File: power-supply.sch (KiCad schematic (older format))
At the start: 90 parts, among them IC1 TPS54561, J11 DC_SOCKET, J12 S2B-PH-K-S_LF__SN_, U10 TPS62823DLCT, U11 TPS62823DLCT, U12 TPS62823DLCT, U13 TPS62823DLCT, U9 LM3881MME_NOPB

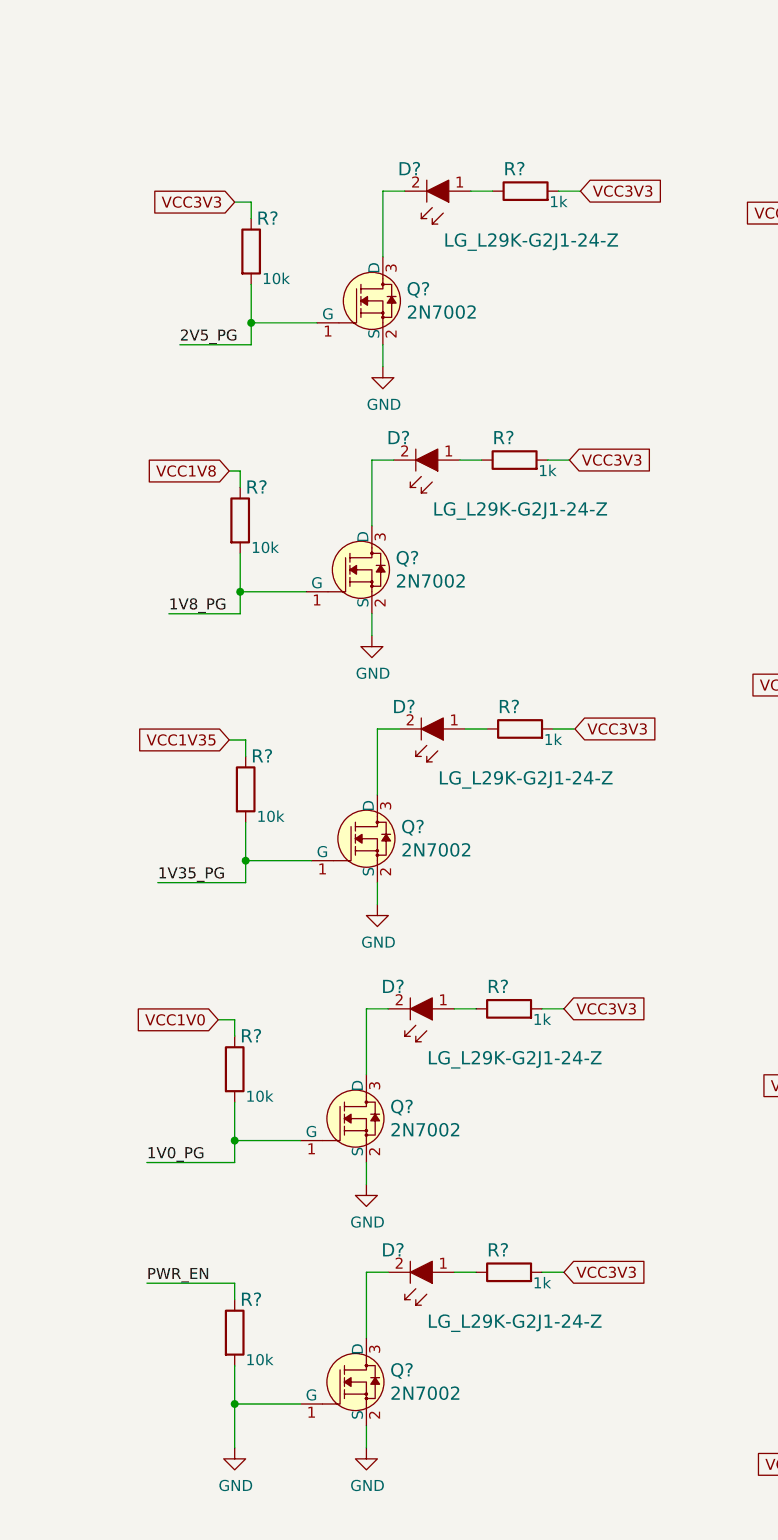
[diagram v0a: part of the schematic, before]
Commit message: Added VRs component placement, fix in 5V0 layout
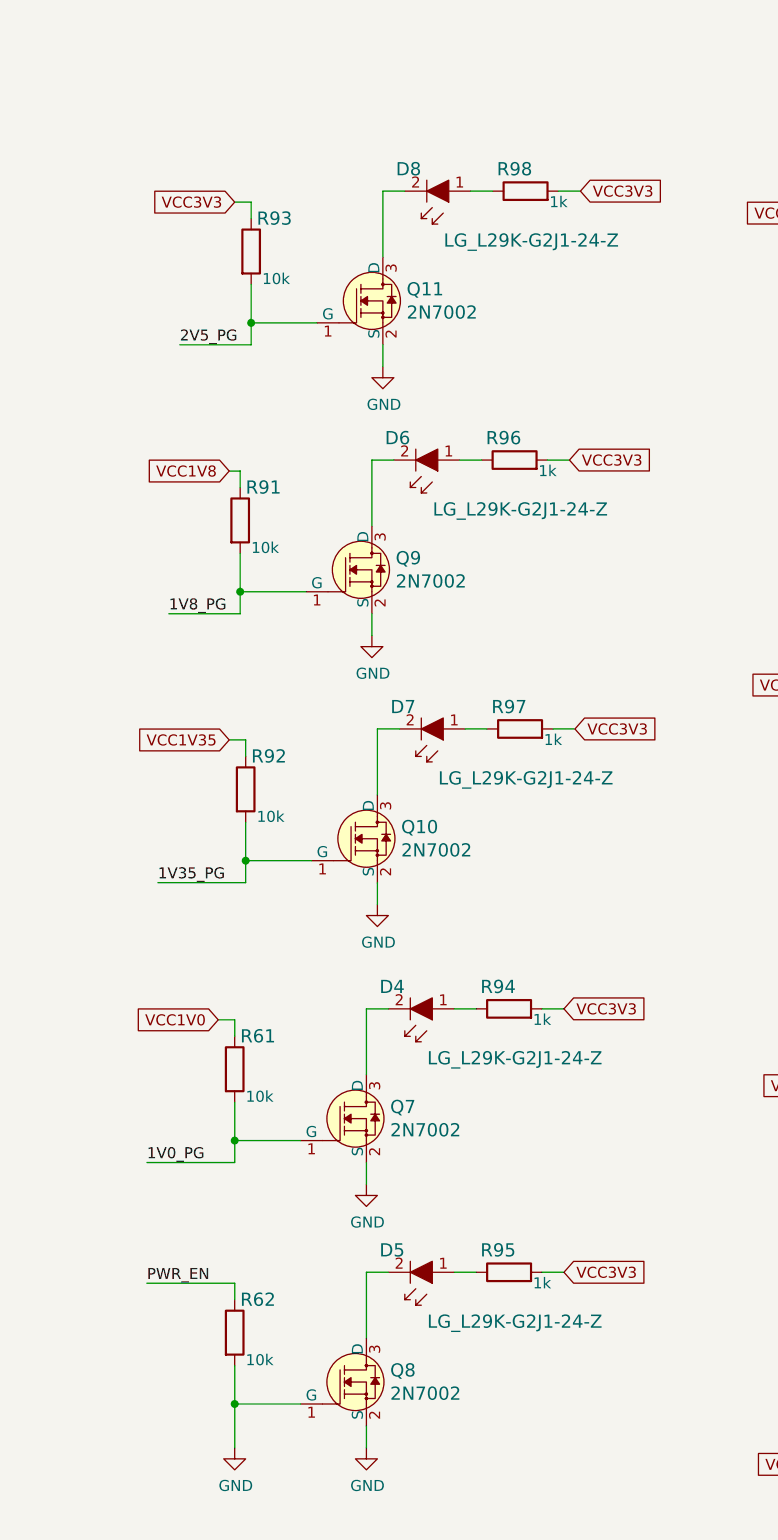
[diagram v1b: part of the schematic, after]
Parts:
- removed R69: R_0R_0402, artix-dc-scm-footprints:0402-res, symbol artix-dc-scm:R_0R_0402
- added R69: R_0R_1206, artix-dc-scm-footprints:1206-res, symbol artix-dc-scm:R_0R_1206
- gave numbers to parts that had none: 28

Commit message: Removed DC connector
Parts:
- removed F2: 0466003.NR, artix-dc-scm-footprints:1206-Fuse-Littelfuse-0466-0-0-MFG, symbol artix-dc-scm:0466003.NR
- removed J11: DC_SOCKET, artix-dc-scm-footprints:DC_SOCKET, symbol artix-dc-scm:DC_SOCKET
- added TP3, TP4: RCW-0C, artix-dc-scm-footprints:PROBE_PAD_1206, symbol artix-dc-scm:RCW-0C
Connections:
- net labels added: P12V_AUX
- net labels removed: PCIe_12V
- wire segments 342 -> 337
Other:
- note added: "External 12V supply"
- note removed: "12V/2.5A\ninput"
- note removed: "fit socket but\nno fuse, optional\nfor PCIe power"
- note removed: "in socket"
- moved on the sheet: F1
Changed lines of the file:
@@
 Comment4 ""
 $EndDescr
-Text GLabel 1350 1975 0    50   Input ~ 0
-PCIe_12V
-Text Notes 1775 1250 0    50   ~ 0
-in socket
-Text Notes 1550 2275 0    50   ~ 0
-fit socket but\nno fuse, optional\nfor PCIe power
-Text Notes 1025 1550 0    50   ~ 0
-12V/2.5A\ninput
 Wire Wire Line
 	12975 2900 12675 2900
@@
 L artix-dc-scm:0466003.NR F1
 U 1 1 5FE8C269
-P 1500 1975
-F 0 "F1" H 1850 2189 50  0000 C CNN
-F 1 "0466003.NR" H 1850 2098 50  0000 C CNN
-F 2 "artix-dc-scm-footprints:1206-Fuse-Littelfuse-0466-0-0-MFG" H 1500 2275 50  0001 L CNN
-F 3 "https://www.littelfuse.com/~/media/electronics/datasheets/fuses/littelfuse_fuse_466_datasheet.pdf.pdf" H 1500 2475 50  0001 L CNN
-F 4 "Littelfuse" H 1500 2475 50  0001 L CNN "Manufacturer"
-F 5 "0466003.NR " H 1750 2375 50  0001 C CNN "MPN"
-	1    1500 1975
-	1    0    0    -1
-$EndComp
-Wire Wire Line
-	2150 1150 2275 1150
-Wire Wire Line
-	1350 1975 1600 1975
-Wire Wire Line
-	2100 1975 2350 1975
-$Comp
-L artix-dc-scm:0466003.NR F2
-U 1 1 5FFF57DB
-P 1550 1150
-F 0 "F2" H 1900 1364 50  0000 C CNN
-F 1 "0466003.NR" H 1900 1273 50  0000 C CNN
-F 2 "artix-dc-scm-footprints:1206-Fuse-Littelfuse-0466-0-0-MFG" H 1550 1450 50  0001 L CNN
-F 3 "https://www.littelfuse.com/~/media/electronics/datasheets/fuses/littelfuse_fuse_466_datasheet.pdf.pdf" H 1550 1650 50  0001 L CNN
-F 4 "Littelfuse" H 1550 1650 50  0001 L CNN "Manufacturer"
-F 5 "0466003.NR " H 1800 1550 50  0001 C CNN "MPN"
-	1    1550 1150
-	1    0    0    -1
-$EndComp
-Text GLabel 2350 1975 2    50   Input ~ 0
+P 1775 2250
+F 0 "F1" H 2125 2464 50  0000 C CNN
+F 1 "0466003.NR" H 2125 2373 50  0000 C CNN
+F 2 "artix-dc-scm-footprints:1206-Fuse-Littelfuse-0466-0-0-MFG" H 1775 2550 50  0001 L CNN
+F 3 "https://www.littelfuse.com/~/media/electronics/datasheets/fuses/littelfuse_fuse_466_datasheet.pdf.pdf" H 1775 2750 50  0001 L CNN
+F 4 "Littelfuse" H 1775 2750 50  0001 L CNN "Manufacturer"
+F 5 "0466003.NR " H 2025 2650 50  0001 C CNN "MPN"
+	1    1775 2250
+	1    0    0    -1
+$EndComp
+Wire Wire Line
+	1625 2250 1875 2250
+Wire Wire Line
+	2375 2250 2625 2250
+Text GLabel 2625 2250 2    50   Input ~ 0
 VCC12V
-Text GLabel 2400 850  2    50   Input ~ 0
-VCC12V
-Wire Wire Line
-	2275 850  2275 1150
-Wire Wire Line
-	2275 850  2400 850
-$Comp
-L artix-dc-scm:GND #PWR049
-U 1 1 60217368
-P 2300 1450
-F 0 "#PWR049" H 2300 1200 50  0001 C CNN
-F 1 "GND" H 2305 1277 50  0000 C CNN
-F 2 "" H 2300 1450 50  0001 C CNN
-F 3 "" H 2300 1450 50  0001 C CNN
-	1    2300 1450
-	1    0    0    -1
-$EndComp
 $Comp
 L artix-dc-scm:TPS54561 IC1
@@
 Text Notes 12900 6375 0    118  ~ 0
 1V35 supply
-$Comp
-L artix-dc-scm:DC_SOCKET J11
-U 1 1 633BB6FF
-P 1250 1250
-F 0 "J11" H 1183 1603 60  0000 C CNN
-F 1 "DC_SOCKET" H 1300 975 60  0001 C CNN
-F 2 "artix-dc-scm-footprints:DC_SOCKET" H 1300 900 60  0001 C CNN
-F 3 "" H 1250 1250 60  0001 C CNN
-F 4 "Multicomp" H 1275 775 50  0001 C CNN "Manufacturer"
-F 5 "MJ-179PH" H 1183 1505 50  0000 C CNN "MPN"
-	1    1250 1250
-	1    0    0    -1
-$EndComp
-Wire Wire Line
-	1650 1150 1450 1150
-Wire Wire Line
-	1450 1350 1550 1350
-Wire Wire Line
-	2300 1350 2300 1450
-Wire Wire Line
-	1450 1250 1550 1250
-Wire Wire Line
-	1550 1250 1550 1350
-Connection ~ 1550 1350
-Wire Wire Line
-	1550 1350 2300 1350
 $Comp
 L artix-dc-scm:IHLP1212AEERR47M11 L2
@@
 	0    1    1    0
 $EndComp
+$Comp
+L artix-dc-scm:RCW-0C TP3
+U 1 1 5FE83A9D
+P 1900 1575
+F 0 "TP3" V 1900 1400 50  0000 C CNN
+F 1 "RCW-0C" V 1766 1622 50  0001 C CNN
+F 2 "artix-dc-scm-footprints:PROBE_PAD_1206" H 2100 1775 60  0001 L CNN
+F 3 "https://www.te.com/commerce/DocumentDelivery/DDEController?Action=srchrtrv&DocNm=1773266&DocType=DS&DocLang=English" H 2100 1875 60  0001 L CNN
+F 4 "RCW-0C" H 2100 2075 60  0001 L CNN "MPN"
+F 5 "TE Connectivity AMP Connectors" H 2100 2675 60  0001 L CNN "Manufacturer"
+	1    1900 1575
+	0    1    1    0
+$EndComp
+$Comp
+L artix-dc-scm:RCW-0C TP4
+U 1 1 5FEA4BA8
+P 1900 1725
+F 0 "TP4" V 1925 1550 50  0000 C CNN
+F 1 "RCW-0C" V 1766 1772 50  0001 C CNN
+F 2 "artix-dc-scm-footprints:PROBE_PAD_1206" H 2100 1925 60  0001 L CNN
+F 3 "https://www.te.com/commerce/DocumentDelivery/DDEController?Action=srchrtrv&DocNm=1773266&DocType=DS&DocLang=English" H 2100 2025 60  0001 L CNN
+F 4 "RCW-0C" H 2100 2225 60  0001 L CNN "MPN"
+F 5 "TE Connectivity AMP Connectors" H 2100 2825 60  0001 L CNN "Manufacturer"
+	1    1900 1725
+	0    1    1    0
+$EndComp
+Text GLabel 2250 1400 1    50   Input ~ 0
+VCC12V
+Wire Wire Line
+	2000 1575 2250 1575
+Wire Wire Line
+	2250 1575 2250 1400
+$Comp
+L artix-dc-scm:GND #PWR?
+U 1 1 5FEC5E7F
+P 2250 1825
+F 0 "#PWR?" H 2250 1575 50  0001 C CNN
+F 1 "GND" H 2255 1652 50  0000 C CNN
+F 2 "" H 2250 1825 50  0001 C CNN
+F 3 "" H 2250 1825 50  0001 C CNN
+	1    2250 1825
+	1    0    0    -1
+$EndComp
+Wire Wire Line
+	2000 1725 2250 1725
+Wire Wire Line
+	2250 1725 2250 1825
+Text GLabel 1625 2250 0    50   Input ~ 0
+P12V_AUX
+Text Notes 1300 925  0    118  ~ 0
+External 12V supply
 $EndSCHEMATC

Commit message: Added PWR_EN optional pullup
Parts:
- added R99: R_1k_0402, artix-dc-scm-footprints:0402-res, symbol artix-dc-scm:R_1k_0402
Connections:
- net labels removed: VCCAUX_EN_N, VCCINT_EN_N, VCCIO_EN_N
- wire segments 337 -> 340
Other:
- note added: "DNP"
- note removed: "TODO: add footprint in libs"
- moved on the sheet: C64, R63, R64, R65, U9
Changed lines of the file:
@@
 Text Notes 1900 6825 0    118  ~ 0
 To CHECK
-Text Label 2700 9775 2    50   ~ 0
+Text Label 3000 9775 2    50   ~ 0
 VCCINT_EN
-Text Label 2700 9875 2    50   ~ 0
+Text Label 3000 9875 2    50   ~ 0
 VCCAUX_EN
 Wire Wire Line
-	2075 10500 2075 10075
+	2375 10500 2375 10075
 $Comp
 L artix-dc-scm:GND #PWR048
 U 1 1 61620212
-P 2075 10500
-F 0 "#PWR048" H 2075 10250 50  0001 C CNN
-F 1 "GND" H 2080 10327 50  0000 C CNN
-F 2 "" H 2075 10500 50  0001 C CNN
-F 3 "" H 2075 10500 50  0001 C CNN
-	1    2075 10500
-	1    0    0    -1
-$EndComp
-Wire Wire Line
-	2075 10075 2000 10075
-Text GLabel 1025 9175 1    50   Input ~ 0
+P 2375 10500
+F 0 "#PWR048" H 2375 10250 50  0001 C CNN
+F 1 "GND" H 2380 10327 50  0000 C CNN
+F 2 "" H 2375 10500 50  0001 C CNN
+F 3 "" H 2375 10500 50  0001 C CNN
+	1    2375 10500
+	1    0    0    -1
+$EndComp
+Wire Wire Line
+	2375 10075 2300 10075
+Text GLabel 1325 9175 1    50   Input ~ 0
 VCC3V3
 Wire Wire Line
-	1200 9775 1025 9775
-Wire Wire Line
-	1025 9175 1025 9775
-Text Label 625  9875 0    50   ~ 0
+	1500 9775 1325 9775
+Wire Wire Line
+	1325 9175 1325 9775
+Text Label 750  9875 0    50   ~ 0
 PWR_EN
 Wire Wire Line
-	625  9875 1200 9875
+	750  9875 1125 9875
 $Comp
 L artix-dc-scm:C_10n_0402 C64
 U 1 1 6204B4B4
-P 800 10275
-F 0 "C64" H 915 10320 60  0000 L CNN
-F 1 "C_10n_0402" H 800 10125 60  0001 C CNN
-F 2 "artix-dc-scm-footprints:0402-cap" H 1000 10475 60  0001 L CNN
-F 3 "" H 800 10275 50  0001 C CNN
-F 4 "AVX" H 1000 10675 60  0001 L CNN "Manufacturer"
-F 5 "04025G103ZAT2A" H 1000 10575 60  0001 L CNN "MPN"
-F 6 "10n" H 915 10222 50  0000 L CNN "Val"
-	1    800  10275
-	1    0    0    -1
-$EndComp
-Wire Wire Line
-	800  9975 1200 9975
+P 1100 10275
+F 0 "C64" H 1215 10320 60  0000 L CNN
+F 1 "C_10n_0402" H 1100 10125 60  0001 C CNN
+F 2 "artix-dc-scm-footprints:0402-cap" H 1300 10475 60  0001 L CNN
+F 3 "" H 1100 10275 50  0001 C CNN
+F 4 "AVX" H 1300 10675 60  0001 L CNN "Manufacturer"
+F 5 "04025G103ZAT2A" H 1300 10575 60  0001 L CNN "MPN"
+F 6 "10n" H 1215 10222 50  0000 L CNN "Val"
+	1    1100 10275
+	1    0    0    -1
+$EndComp
+Wire Wire Line
+	1100 9975 1500 9975
 $Comp
 L artix-dc-scm:GND #PWR047
 U 1 1 6211AF82
-P 800 10525
-F 0 "#PWR047" H 800 10275 50  0001 C CNN
-F 1 "GND" H 805 10352 50  0000 C CNN
-F 2 "" H 800 10525 50  0001 C CNN
-F 3 "" H 800 10525 50  0001 C CNN
-	1    800  10525
+P 1100 10525
+F 0 "#PWR047" H 1100 10275 50  0001 C CNN
+F 1 "GND" H 1105 10352 50  0000 C CNN
+F 2 "" H 1100 10525 50  0001 C CNN
+F 3 "" H 1100 10525 50  0001 C CNN
+	1    1100 10525
 	1    0    0    -1
 $EndComp
@@
 Wire Notes Line
 	475  8400 475  8425
-Text Label 2700 9975 2    50   ~ 0
+Text Label 3000 9975 2    50   ~ 0
 VCCIO_EN
 Text Notes 12875 2350 0    118  ~ 0
@@
 L artix-dc-scm:LM3881MME_NOPB U9
 U 1 1 6113B8AB
-P 1600 9875
-F 0 "U9" H 1350 10200 50  0000 C CNN
-F 1 "LM3881MME_NOPB" H 1675 10150 50  0000 C CNN
-F 2 "artix-dc-scm-footprints:VSSOP8-Texas_Instruments-DGK0008A" H 1600 10275 50  0001 L CNN
-F 3 "http://www.ti.com/lit/ds/symlink/lm3881.pdf" H 1600 10375 50  0001 L CNN
-F 4 "Texas Instruments" H 1600 10475 50  0001 L CNN "Manufacturer"
-F 5 "LM3881MME/NOPB" H 1950 10375 50  0001 C CNN "MPN"
-	1    1600 9875
-	1    0    0    -1
-$EndComp
-Wire Wire Line
-	2000 9975 2275 9975
-Wire Wire Line
-	2000 9875 2175 9875
-Wire Wire Line
-	2000 9775 2075 9775
+P 1900 9875
+F 0 "U9" H 1650 10200 50  0000 C CNN
+F 1 "LM3881MME_NOPB" H 1975 10150 50  0000 C CNN
+F 2 "artix-dc-scm-footprints:VSSOP8-Texas_Instruments-DGK0008A" H 1900 10275 50  0001 L CNN
+F 3 "http://www.ti.com/lit/ds/symlink/lm3881.pdf" H 1900 10375 50  0001 L CNN
+F 4 "Texas Instruments" H 1900 10475 50  0001 L CNN "Manufacturer"
+F 5 "LM3881MME/NOPB" H 2250 10375 50  0001 C CNN "MPN"
+	1    1900 9875
+	1    0    0    -1
+$EndComp
+Wire Wire Line
+	2300 9975 2575 9975
+Wire Wire Line
+	2300 9875 2475 9875
+Wire Wire Line
+	2300 9775 2375 9775
 Text Notes 1025 6650 0    118  ~ 0
 Power sequencer
@@
 ^ TODO: decide which DC-SCI pin connected\n    to FPGA does this
 Wire Wire Line
-	800  9975 800  10125
-Wire Wire Line
-	800  10425 800  10525
-Wire Wire Line
-	1200 10075 1025 10075
-Wire Wire Line
-	1025 10075 1025 9775
-Connection ~ 1025 9775
+	1100 9975 1100 10125
+Wire Wire Line
+	1100 10425 1100 10525
+Wire Wire Line
+	1500 10075 1325 10075
+Wire Wire Line
+	1325 10075 1325 9775
+Connection ~ 1325 9775
 $Comp
 L artix-dc-scm:R_1k_0402 R63
 U 1 1 5FFECF1E
-P 2075 9450
-F 0 "R63" V 2030 9520 60  0000 L CNN
-F 1 "R_1k_0402" H 2075 9300 60  0001 C CNN
-F 2 "artix-dc-scm-footprints:0402-res" H 2275 9650 60  0001 L CNN
-F 3 "" H 2075 9450 50  0001 C CNN
-F 4 "BOURNS" H 2275 9850 60  0001 L CNN "Manufacturer"
-F 5 "CR0402-FX-1001GLF" H 2275 9750 60  0001 L CNN "MPN"
-F 6 "1k" V 2128 9520 50  0000 L CNN "Val"
-	1    2075 9450
+P 2375 9450
+F 0 "R63" V 2330 9520 60  0000 L CNN
+F 1 "R_1k_0402" H 2375 9300 60  0001 C CNN
+F 2 "artix-dc-scm-footprints:0402-res" H 2575 9650 60  0001 L CNN
+F 3 "" H 2375 9450 50  0001 C CNN
+F 4 "BOURNS" H 2575 9850 60  0001 L CNN "Manufacturer"
+F 5 "CR0402-FX-1001GLF" H 2575 9750 60  0001 L CNN "MPN"
+F 6 "1k" V 2428 9520 50  0000 L CNN "Val"
+	1    2375 9450
 	0    1    1    0
 $EndComp
@@
 L artix-dc-scm:R_1k_0402 R64
 U 1 1 5FFED382
-P 2175 9450
-F 0 "R64" V 2130 9520 60  0000 L CNN
-F 1 "R_1k_0402" H 2175 9300 60  0001 C CNN
-F 2 "artix-dc-scm-footprints:0402-res" H 2375 9650 60  0001 L CNN
-F 3 "" H 2175 9450 50  0001 C CNN
-F 4 "BOURNS" H 2375 9850 60  0001 L CNN "Manufacturer"
-F 5 "CR0402-FX-1001GLF" H 2375 9750 60  0001 L CNN "MPN"
-F 6 "1k" V 2228 9520 50  0000 L CNN "Val"
-	1    2175 9450
+P 2475 9450
+F 0 "R64" V 2430 9520 60  0000 L CNN
+F 1 "R_1k_0402" H 2475 9300 60  0001 C CNN
+F 2 "artix-dc-scm-footprints:0402-res" H 2675 9650 60  0001 L CNN
+F 3 "" H 2475 9450 50  0001 C CNN
+F 4 "BOURNS" H 2675 9850 60  0001 L CNN "Manufacturer"
+F 5 "CR0402-FX-1001GLF" H 2675 9750 60  0001 L CNN "MPN"
+F 6 "1k" V 2528 9520 50  0000 L CNN "Val"
+	1    2475 9450
 	0    1    1    0
 $EndComp
@@
 L artix-dc-scm:R_1k_0402 R65
 U 1 1 5FFED63B
-P 2275 9450
-F 0 "R65" V 2230 9520 60  0000 L CNN
-F 1 "R_1k_0402" H 2275 9300 60  0001 C CNN
-F 2 "artix-dc-scm-footprints:0402-res" H 2475 9650 60  0001 L CNN
-F 3 "" H 2275 9450 50  0001 C CNN
-F 4 "BOURNS" H 2475 9850 60  0001 L CNN "Manufacturer"
-F 5 "CR0402-FX-1001GLF" H 2475 9750 60  0001 L CNN "MPN"
-F 6 "1k" V 2328 9520 50  0000 L CNN "Val"
-	1    2275 9450
-	0    1    1    0
-$EndComp
-Wire Wire Line
-	2075 9600 2075 9775
-Connection ~ 2075 9775
-Wire Wire Line
-	2075 9775 2700 9775
-Wire Wire Line
-	2175 9600 2175 9875
-Connection ~ 2175 9875
-Wire Wire Line
-	2175 9875 2700 9875
-Wire Wire Line
-	2275 9600 2275 9975
-Connection ~ 2275 9975
-Wire Wire Line
-	2275 9975 2700 9975
-Wire Wire Line
-	2075 9300 2075 9225
-Wire Wire Line
-	2075 9225 2175 9225
-Wire Wire Line
-	2275 9225 2275 9300
-Wire Wire Line
-	2175 9300 2175 9225
-Connection ~ 2175 9225
-Wire Wire Line
-	2175 9225 2275 9225
-Wire Wire Line
-	2175 9150 2175 9225
-Text GLabel 2175 9150 1    50   Input ~ 0
+P 2575 9450
+F 0 "R65" V 2530 9520 60  0000 L CNN
+F 1 "R_1k_0402" H 2575 9300 60  0001 C CNN
+F 2 "artix-dc-scm-footprints:0402-res" H 2775 9650 60  0001 L CNN
+F 3 "" H 2575 9450 50  0001 C CNN
+F 4 "BOURNS" H 2775 9850 60  0001 L CNN "Manufacturer"
+F 5 "CR0402-FX-1001GLF" H 2775 9750 60  0001 L CNN "MPN"
+F 6 "1k" V 2628 9520 50  0000 L CNN "Val"
+	1    2575 9450
+	0    1    1    0
+$EndComp
+Wire Wire Line
+	2375 9600 2375 9775
+Connection ~ 2375 9775
+Wire Wire Line
+	2375 9775 3000 9775
+Wire Wire Line
+	2475 9600 2475 9875
+Connection ~ 2475 9875
+Wire Wire Line
+	2475 9875 3000 9875
+Wire Wire Line
+	2575 9600 2575 9975
+Connection ~ 2575 9975
+Wire Wire Line
+	2575 9975 3000 9975
+Wire Wire Line
+	2375 9300 2375 9225
+Wire Wire Line
+	2375 9225 2475 9225
+Wire Wire Line
+	2575 9225 2575 9300
+Wire Wire Line
+	2475 9300 2475 9225
+Connection ~ 2475 9225
+Wire Wire Line
+	2475 9225 2575 9225
+Wire Wire Line
+	2475 9150 2475 9225
+Text GLabel 2475 9150 1    50   Input ~ 0
 VCC3V3
 Wire Wire Line
@@
 	5700 6650 6150 6650
 Text Label 6125 7250 2    50   ~ 0
-VCCIO_EN_N
+VCCIO_EN
 Text Label 6150 8450 2    50   ~ 0
-VCCAUX_EN_N
+VCCAUX_EN
 Text Label 6150 9050 2    50   ~ 0
-VCCINT_EN_N
+VCCINT_EN
 Text Label 6125 7850 2    50   ~ 0
-VCCAUX_EN_N
+VCCAUX_EN
 Text Label 6125 6650 2    50   ~ 0
-VCCIO_EN_N
+VCCIO_EN
 Text GLabel 6225 9350 0    50   Input ~ 0
 VCC1V8
@@
 	5700 9650 6150 9650
 Text Label 6125 9650 2    50   ~ 0
-VCCIO_EN_N
+VCCIO_EN
 Wire Wire Line
 	4475 9775 4475 9850
@@
 Wire Wire Line
 	4175 8875 3275 8875
-Text Notes 3175 9650 0    50   ~ 0
-TODO: add footprint in libs
+Text Notes 1025 9600 1    50   ~ 0
+DNP
 Text Notes 3475 8700 0    50   ~ 0
 RoT booted flag pin
@@
 	2250 1575 2250 1400
 $Comp
-L artix-dc-scm:GND #PWR?
+L artix-dc-scm:GND #PWR0109
 U 1 1 5FEC5E7F
 P 2250 1825
-F 0 "#PWR?" H 2250 1575 50  0001 C CNN
+F 0 "#PWR0109" H 2250 1575 50  0001 C CNN
 F 1 "GND" H 2255 1652 50  0000 C CNN
 F 2 "" H 2250 1825 50  0001 C CNN
@@
 Text Notes 1300 925  0    118  ~ 0
 External 12V supply
+$Comp
+L artix-dc-scm:R_1k_0402 R99
+U 1 1 6003348A
+P 1125 9500
+F 0 "R99" V 1080 9570 60  0000 L CNN
+F 1 "R_1k_0402" H 1125 9350 60  0001 C CNN
+F 2 "artix-dc-scm-footprints:0402-res" H 1325 9700 60  0001 L CNN
+F 3 "" H 1125 9500 50  0001 C CNN
+F 4 "BOURNS" H 1325 9900 60  0001 L CNN "Manufacturer"
+F 5 "CR0402-FX-1001GLF" H 1325 9800 60  0001 L CNN "MPN"
+F 6 "1k" V 1178 9570 50  0000 L CNN "Val"
+	1    1125 9500
+	0    1    1    0
+$EndComp
+Wire Wire Line
+	1125 9650 1125 9875
+Connection ~ 1125 9875
+Wire Wire Line
+	1125 9875 1500 9875
+Wire Wire Line
+	1125 9350 1125 9175
+Text GLabel 1125 9175 1    50   Input ~ 0
+VCC3V3
 $EndSCHEMATC
